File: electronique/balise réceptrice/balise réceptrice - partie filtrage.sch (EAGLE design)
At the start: 35 parts, among them IC1 TL084P, IC2 TL084P, IC3 TL084P

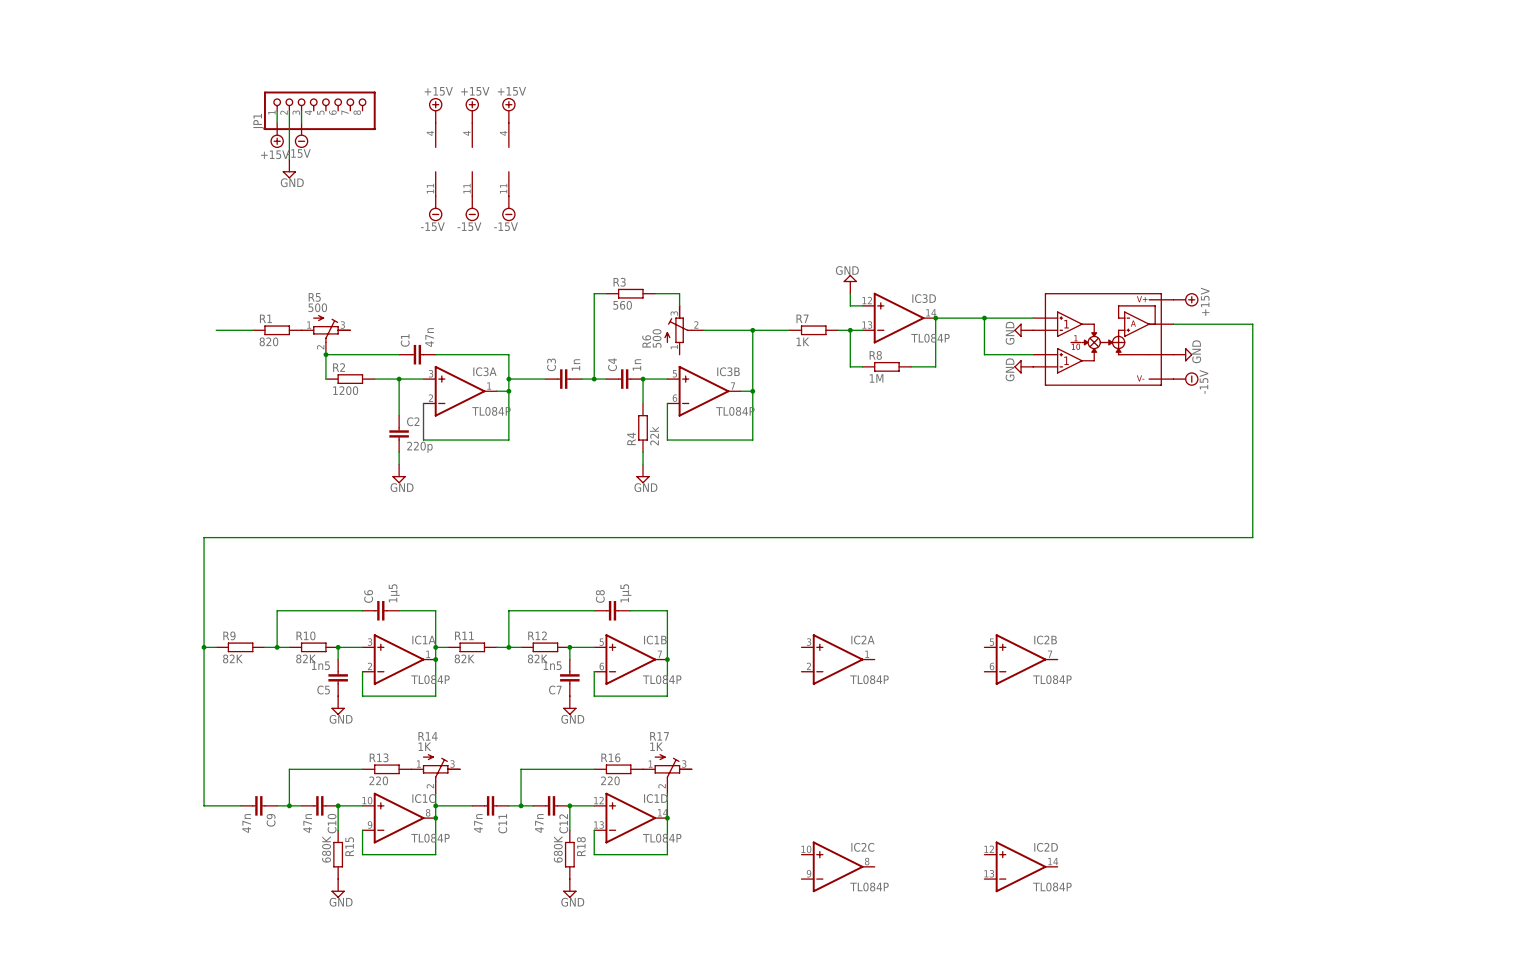
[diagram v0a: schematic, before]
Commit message: maj filtrage + ajout routage balise receptrice, partie filtrage
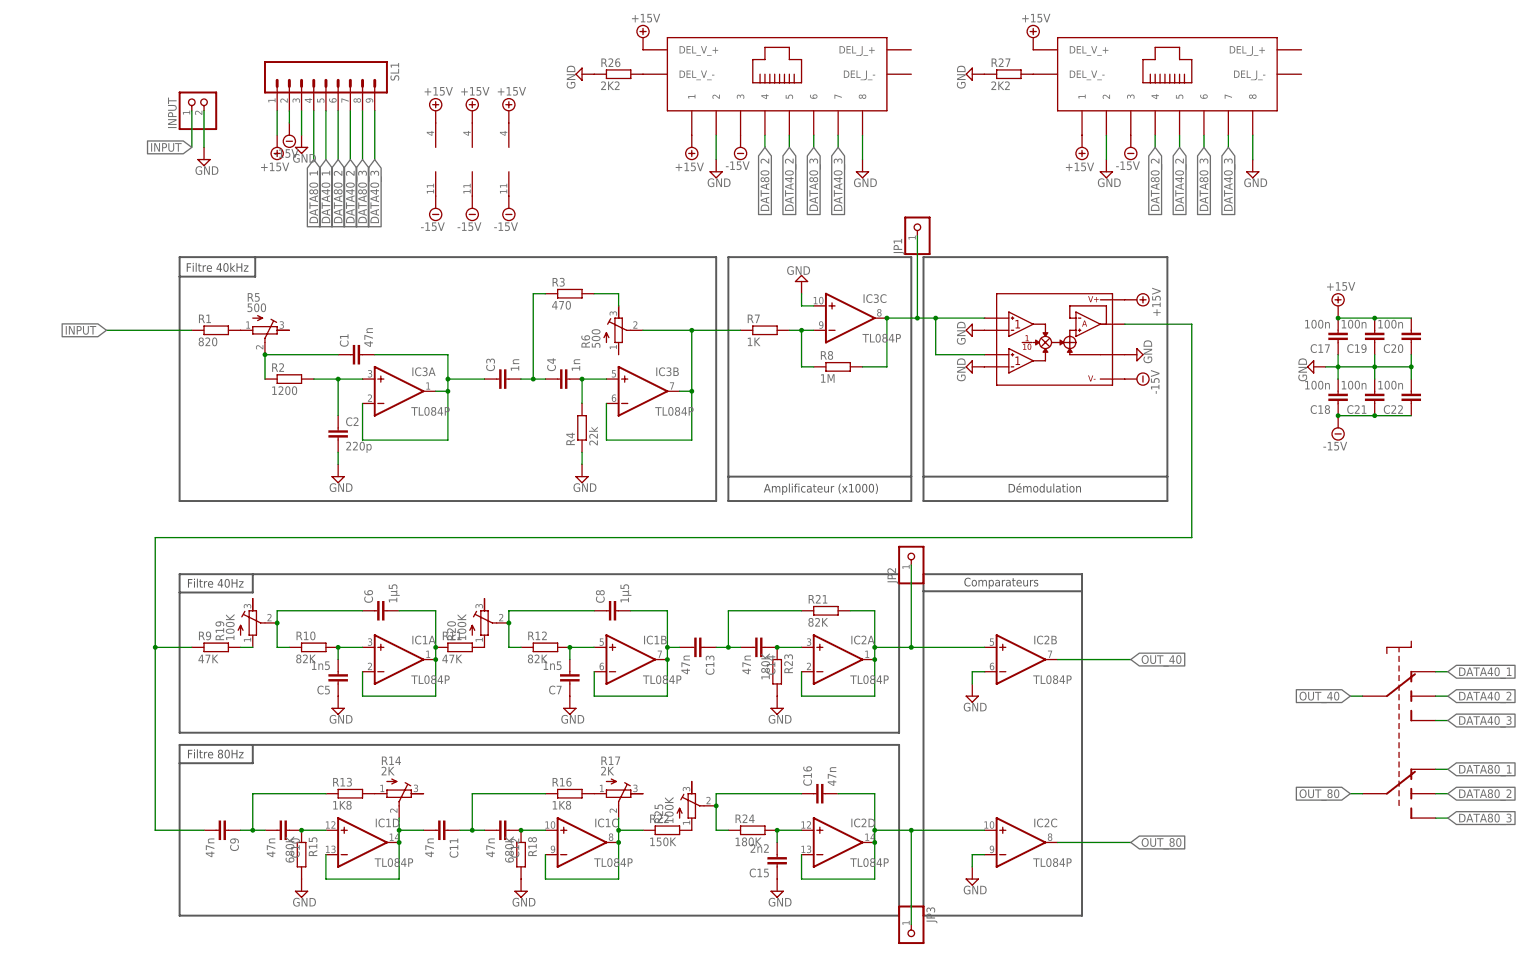
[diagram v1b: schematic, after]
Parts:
- added C13, C14, C16: 47n, resistor:C-EU050-024X044
- added C15: 2n2, resistor:C-EU050-024X044
- added C17, C18, C19, C20, C21, C22: 100n, resistor:C-EU050-024X044
- added INPUT: (no value), pinhead:PINHD-1X2
- added JP2, JP3: (no value), pinhead:PINHD-1X1
- added R19, R20, R25: 100K, resistor:R-TRIMM3339P
- added R21: 82K, resistor:R-EU_0207/2V
- added R22: 150K, resistor:R-EU_0207/2V
- added R23, R24: 180K, resistor:R-EU_0207/2V
- added R26, R27: 2K2, resistor:R-EU_0207/2V
- added SL1: (no value), con-amp-quick:M09
- added U$2, U$3: RJ45_FEMELLE, libINTech-Balise:RJ45_FEMELLE
- added U$4: SWITCH_DP3T_SP112, libINTech-Balise:SWITCH_DP3T_SP112
- JP1: device pinhead:PINHD-1X8 -> pinhead:PINHD-1X1
- R1, R12, R15, R18, R2, R4: device resistor:R-EU_0204/7 -> resistor:R-EU_0207/2V
- R11: value 82K -> 47K; device resistor:R-EU_0204/7 -> resistor:R-EU_0207/2V
- R13, R16: value 220 -> 1K8; device resistor:R-EU_0204/7 -> resistor:R-EU_0207/2V
- R14, R17: value 1K -> 2K
- R3: value 560 -> 470; device resistor:R-EU_0204/7 -> resistor:R-EU_0207/2V
- R9: value 82K -> 47K
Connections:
- new net DATA40_1: SL1.5, U$4.1A
- new net DATA40_2: SL1.7, U$2.5, U$3.5, U$4.1B
- new net DATA40_3: SL1.9, U$2.7, U$3.7, U$4.1C
- new net DATA80_1: SL1.4, U$4.2A
- new net DATA80_2: SL1.6, U$2.4, U$3.4, U$4.2B
- new net DATA80_3: SL1.8, U$2.6, U$3.6, U$4.2C
- new net INPUT: INPUT.1, R1.1
- new net N$27: R19.E, R9.2
- new net N$28: R11.2, R20.E
- new net N$29: C16.1, R24.1, R25.S
- new net N$30: C15.2, IC2D.+IN, R24.2
- new net N$31: C13.1, C14.2, R21.1
- new net N$32: IC2A.-IN, IC2A.OUT, IC2B.+IN, JP2.1, R21.2
- new net N$33: C14.1, IC2A.+IN, R23.1
- new net N$34: C16.2, IC2C.+IN, IC2D.-IN, IC2D.OUT, JP3.1
- new net N$35: R22.2, R25.E
- new net N$36: R27.2, U$3.DEL_V_-
- new net OUT_40: IC2B.OUT, U$4.COM1
- new net OUT_80: IC2C.OUT, U$4.COM2
- net +15V: now also C17.2, C19.2, C20.2, SL1.1, U$2.1, U$2.DEL_V_+, U$3.1, U$3.DEL_V_+; no longer JP1.1
- net -15V: now also C18.1, C21.1, C22.1, SL1.2, U$2.3, U$3.3; no longer JP1.3
- net GND: now also C15.1, C17.1, C18.2, C19.1, C20.1, C21.2, C22.2, IC2B.-IN, IC2C.-IN, IC3C.+IN, INPUT.2, R23.2, R26.1, R27.1, SL1.3, U$2.2, U$2.8, U$3.2, U$3.8; no longer IC3D.+IN, JP1.2
- net N$11: now also R26.2, U$2.DEL_V_-; no longer R1.1
- net N$12: now also R19.S; no longer R9.2
- net N$16: now also R20.S; no longer R11.2
- net N$18: now also C13.2
- net N$2: now also IC3C.-IN; no longer IC3D.-IN
- net N$20: now also IC1D.-IN, IC1D.OUT; no longer IC1C.-IN, IC1C.OUT
- net N$21: now also IC1D.+IN; no longer IC1C.+IN
- net N$24: now also IC1C.-IN, IC1C.OUT, R22.1; no longer IC1D.-IN, IC1D.OUT
- net N$25: now also IC1C.+IN; no longer IC1D.+IN
- net N$3: now also IC3C.OUT, JP1.1; no longer IC3D.OUT
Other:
- note added: "Amplificateur (x1000)"
- note added: "Comparateurs"
- note added: "Démodulation"
- note added: "Filtre 40Hz"
- note added: "Filtre 40kHz"
- note added: "Filtre 80Hz"
- moved on the sheet: C1, C10, C11, C12, C2, C3, C4, C9, IC1C, IC1D, IC2C, IC2D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

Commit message: derniere carte elec : la puissance et la communication sans fil + maj modele 3D balise receptrice
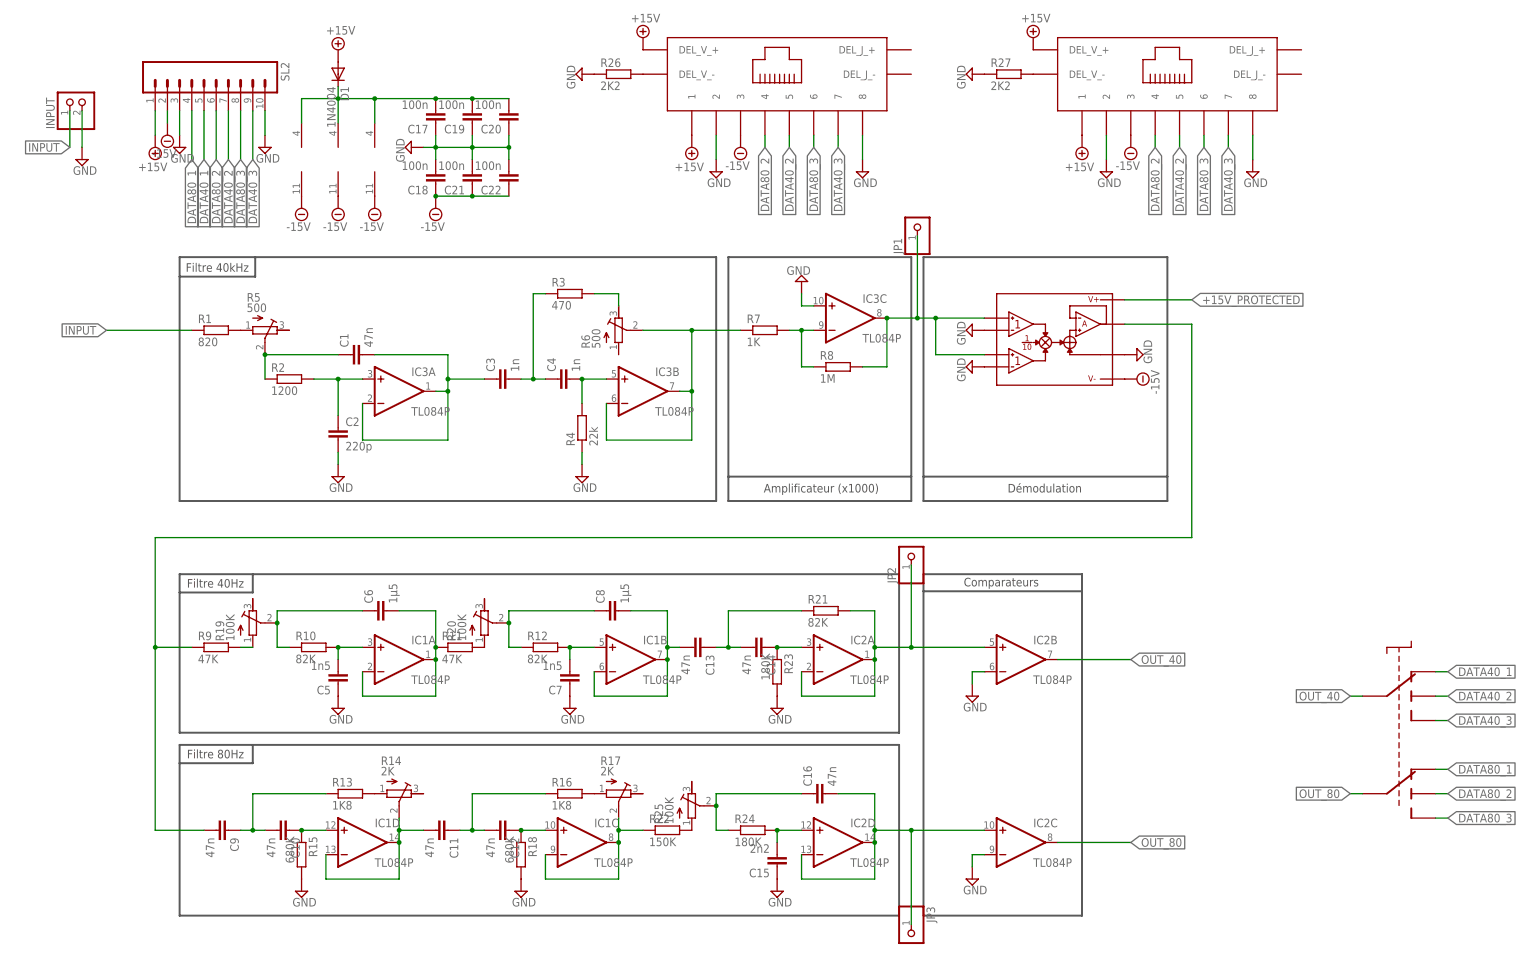
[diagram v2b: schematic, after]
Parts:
- removed SL1: (no value), con-amp-quick:M09
- added D1: 1N4004, diode:1N4004
- added SL2: (no value), con-amp-quick:M10
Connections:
- new net +15V_PROTECTED: C17.2, C19.2, C20.2, D1.C, IC1P.V+, IC2P.V+, IC3P.V+, U$1.+V
- net +15V: now also D1.A, SL2.1; no longer C17.2, C19.2, C20.2, IC1P.V+, IC2P.V+, IC3P.V+, SL1.1, U$1.+V
- net -15V: now also SL2.2; no longer SL1.2
- net DATA40_1: now also SL2.5; no longer SL1.5
- net DATA40_2: now also SL2.7; no longer SL1.7
- net DATA40_3: now also SL2.9; no longer SL1.9
- net DATA80_1: now also SL2.4; no longer SL1.4
- net DATA80_2: now also SL2.6; no longer SL1.6
- net DATA80_3: now also SL2.8; no longer SL1.8
- net GND: now also SL2.10, SL2.3; no longer SL1.3
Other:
- moved on the sheet: C17, C18, C19, C20, C21, C22, INPUT

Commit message: maj liste des composants
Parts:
- C1, C10, C11, C12, C13, C14, C15, C16, C17, C18, C19, C20, C21, C22, C3, C4, C5, C6, C7, C8, C9, D1, IC1, IC2, IC3, INPUT, JP1, JP2, JP3, R1, R10, R11, R12, R13, R14, R15, R16, R17, R18, R19, R2, R20, R21, R22, R23, R24, R25, R26, R27, R3, R4, R5, R6, R7, R8, R9, SL2, U$1, U$2, U$3, U$4: OC_FARNELL (none) -> unknown
- C2: MF (none) -> SUSUMU; MPN (none) -> RR1220P-104-B-T5; OC_FARNELL (none) -> 1653285
